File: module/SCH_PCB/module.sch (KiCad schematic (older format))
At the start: 8 parts, among them J1 Umin ... Umax, M1 HOLE, M2 HOLE, M3 HOLE, M4 HOLE

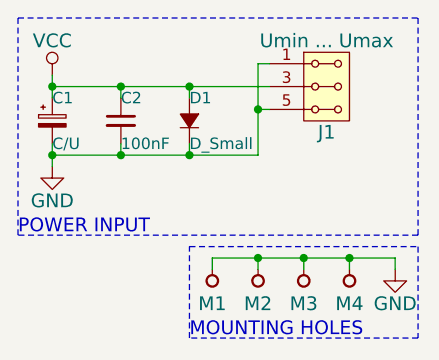
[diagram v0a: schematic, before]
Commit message: FIX: wrong polarised protection diode reversed.
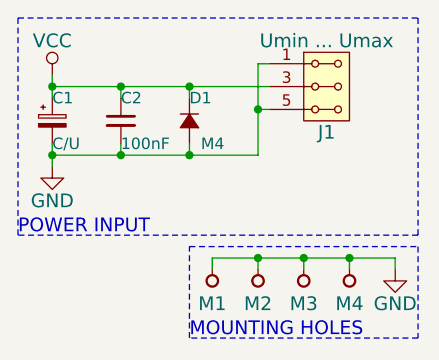
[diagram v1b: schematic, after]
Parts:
- D1: value D_Small -> M4
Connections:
- net GND: now also D1.2 (A); no longer D1.1 (K)
- net VCC: now also D1.1 (K); no longer D1.2 (A)
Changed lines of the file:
@@
 LIBS:elec-unifil
 LIBS:ESD_Protection
-LIBS:freescale
 LIBS:ftdi
 LIBS:gennum
@@
 LIBS:microchip_pic32mcu
 LIBS:microcontrollers
-LIBS:mlab_header
-LIBS:mlab_mechanical
 LIBS:motor_drivers
 LIBS:motorola
@@
 U 1 1 55622FB7
 P 9950 1200
-F 0 "D1" V 10050 1200 50  0000 R CNN
-F 1 "D_Small" V 9850 1200 50  0000 R CNN
+F 0 "D1" V 9850 1200 50  0000 R CNN
+F 1 "M4" V 10050 1150 50  0000 R CNN
 F 2 "" V 9950 1200 60  0000 C CNN
 F 3 "" V 9950 1200 60  0000 C CNN
 	1    9950 1200
-	0    -1   -1   0
+	0    -1   1    0
 $EndComp
 $Comp
